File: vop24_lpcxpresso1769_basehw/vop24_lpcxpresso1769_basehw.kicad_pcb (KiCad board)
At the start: 2 copper layers, 105 x 150 mm, 114 parts, among them J1 Micro_SD_Card, J101 Conn_01x03_Male, J201 Screw_Terminal_01x02, J301 USB_B_Micro, J302 Conn_01x06_Male, J303 Conn_01x05_Male, J304 Screw_Terminal_01x02, J401 Conn_01x02, J402 Conn_01x02, J403 Conn_01x02, J404 Conn_01x04, J405 Conn_01x04, J406 Conn_01x04, U1 LPCXpresso1769, U101 MCP1700T-3302E_TT, U102 MCP1700T-3302E_TT, U103 TPS63001, U201 LM358, U301 TPD4S014, U302 LTC4411, U303 LT1512, U401 ADS1292, U402 LM334, U403 LM334, U404 LM334

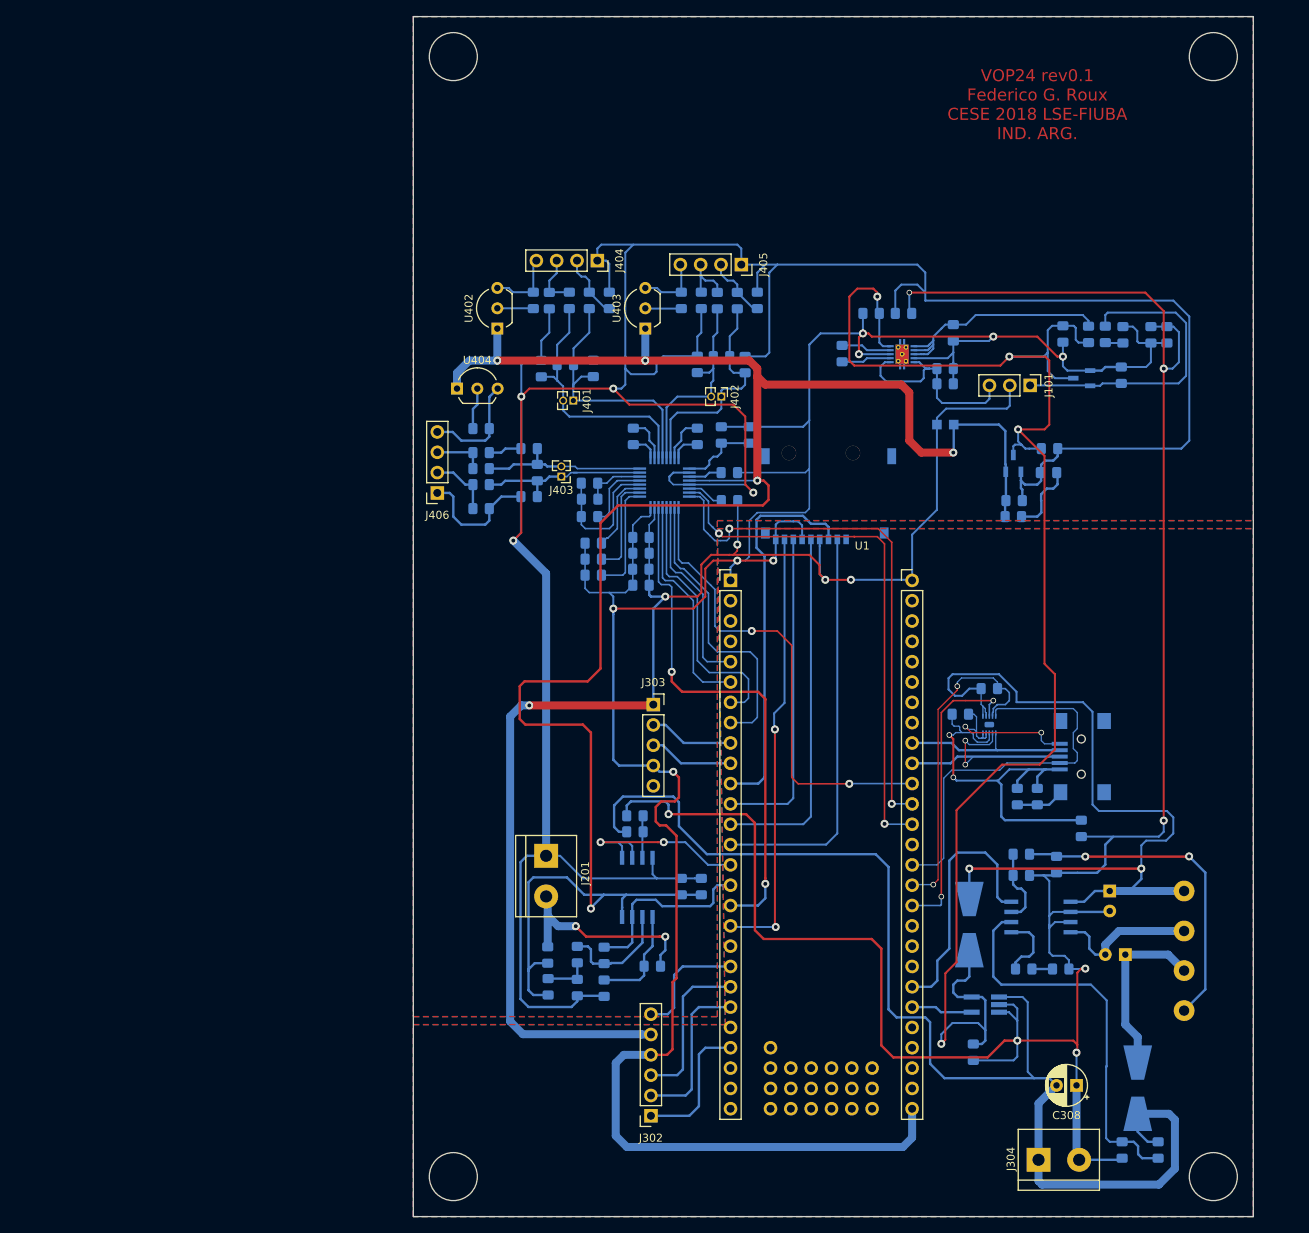
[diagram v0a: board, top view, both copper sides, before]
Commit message: Agregado de leyendas en PCB y ESQ. Agregado de cotas en PCB
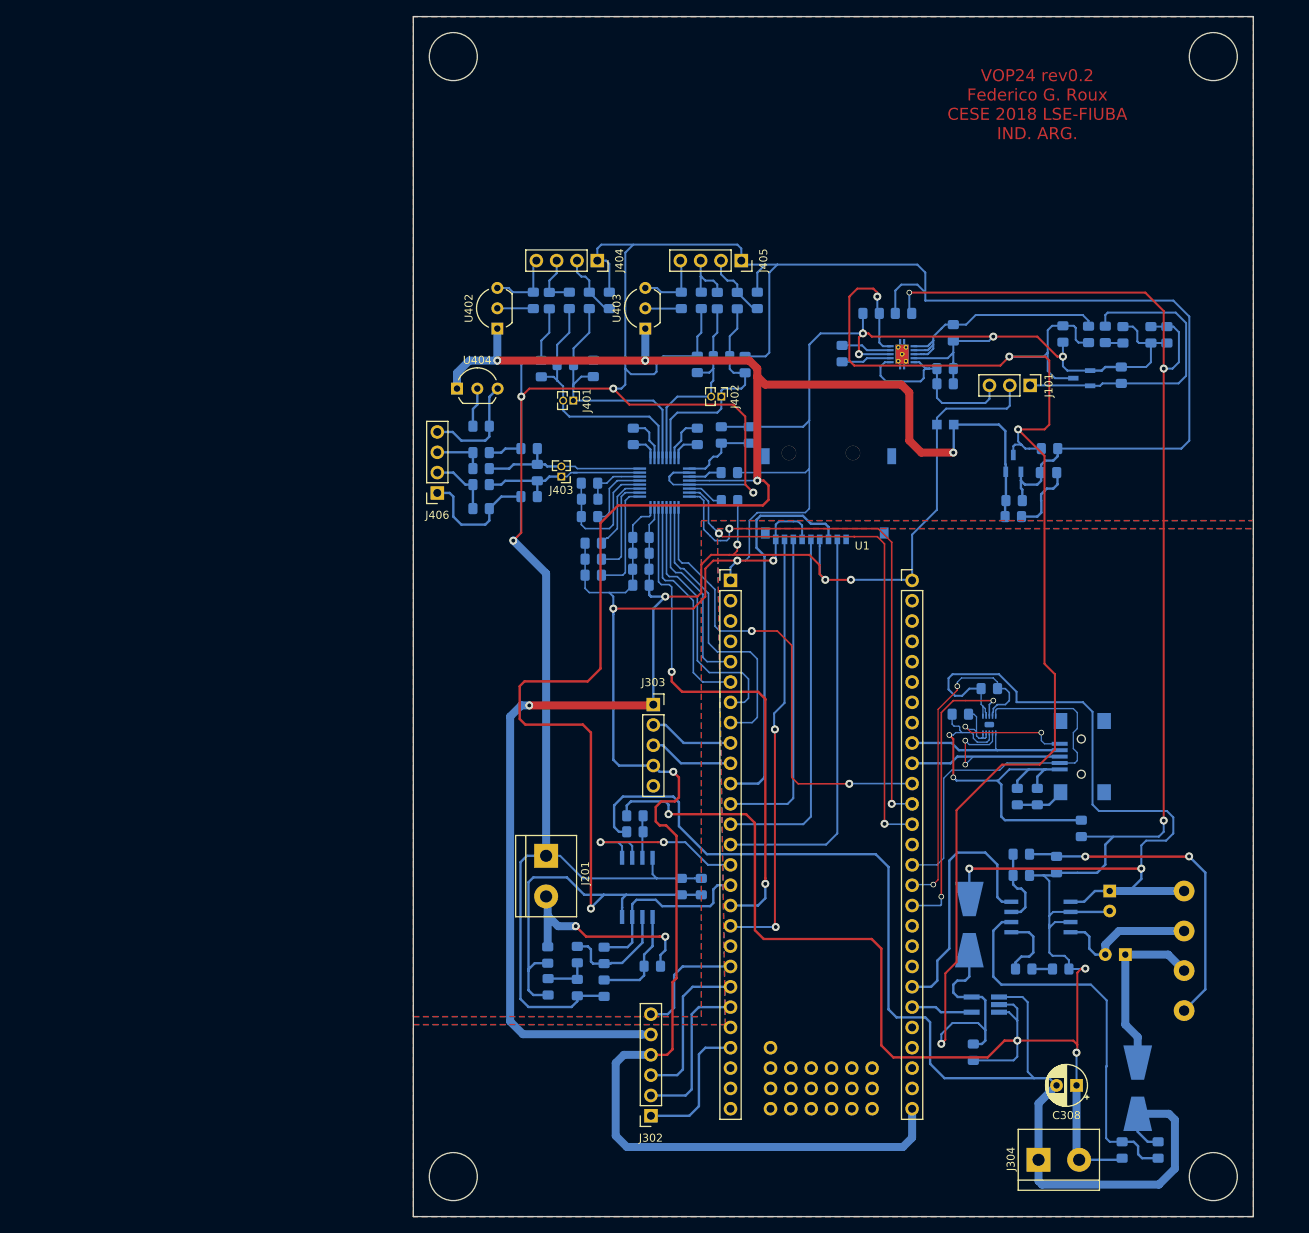
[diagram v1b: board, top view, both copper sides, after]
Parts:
- moved J405 0.50 mm to (81.0, 65.5)
- moved R408 0.30 mm to (48.5, 86.2)
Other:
- board text added: "NOTA SERIGRAFÍA: Como se menciona más arriba, este primer diseño es para realizar en un ROUTER CNC, por lo que no se le dió mucha importancia a la capa de serigrafía porque no se va a realizar. En el diseño final se ubicarán las leyendas de los componentes de una forma más prolija."
- board text added: "NOTA UBICACIÓN COMPONENTES: Los componentes están agrupados por módulo para poder que sea más fácil la inspección a la hora de hacer pruebas, ya que se trata de un prototipo. Además, el hecho de trabajar alrededor de un LPCXpresso hace que el diseño sea más limitado y de mucho mayor tamaño que lo que debería ocupar."
- board text added: "NOTAS CONECTORES: Los conectores J301 y J302 son tiras de pines para conectar directamente los modulos UART-TTL y UART-BLE. No se ubican sobre el borde para que no sobresalgan estas placas hacia afuera, o sobresalgan lo menos posible. El conector miniUSB se ubica lo más cerca del LPCXpresso posible, ya que la conexión no es directa sino a través del STICK, y eso complica la señal de alta velocida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"
- board text added: "NOTAS DE FABRICACION: Este prototipo está diseñado para ser fabricado en un CNC Router para probar las conexiones de cada uno de los módulos. Por ello se usó un solo lado para soldar componentes y minimizar la cantidad de vías. En el siguiente diseño se hará para fabricar en Mayer o Inarci, y se colocará el microcontrolador en lugar del LPCXpresso"
- board text added: "NOTAS DRC: Solamente se marcan los pines no conectados del SHIELD del conector USB, que están cortocircuitados internamente"
- board text added: "TAMAÑO DE PISTAS, VIAS y CLEARANCE: Se crearon las Reglas de Diseño de acuerdo a los estándares de Mayer de 12-10-8-6 mils que se vieron en la cátedra. La mayor parte de la placa está resuelta en el estándar de 8 mils, y en donde se puede, se usaron pistas más grandes."
- board text added: "VOP24 rev0.2 Federico G. Roux CESE 2018 LSE-FIUBA IND. ARG."
- board text removed: "VOP24 rev0.1 Federico G. Roux CESE 2018 LSE-FIUBA IND. ARG."

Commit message: actualizacion de PCB con cambios de ESQ
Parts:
- removed J303: Conn_01x05_Male, Connector_PinSocket_2.54mm:PinSocket_1x05_P2.54mm_Vertical
- removed J304: Screw_Terminal_01x02, TerminalBlock:TerminalBlock_bornier-2_P5.08mm
- removed R101, R102, R103, R303: 0, Resistor_SMD:R_0805_2012Metric_Pad1.15x1.40mm_HandSolder
- added J2: Conn_01x05_Male, Connector_PinSocket_2.54mm:PinSocket_1x05_P2.54mm_Vertical, F.Cu at (-4.67, 125.5)
- added J3: Conn_01x06_Male, Connector_PinSocket_2.54mm:PinSocket_1x06_P2.54mm_Vertical, F.Cu at (-8.27, 125.5)
- added NT101: Net-Tie_2, NetTie:NetTie-2_SMD_Pad0.5mm, F.Cu at (23.8, 126.5)
- added NT102: Net-Tie_2, NetTie:NetTie-2_SMD_Pad0.5mm, F.Cu at (23.8, 124.6)
- added NT103: Net-Tie_2, NetTie:NetTie-2_SMD_Pad0.5mm, F.Cu at (28.2, 124.6)
- added NT301: Net-Tie_2, NetTie:NetTie-2_SMD_Pad0.5mm, F.Cu at (23.8, 133.1)
- added NT302: Net-Tie_2, NetTie:NetTie-2_SMD_Pad0.5mm, F.Cu at (23.8, 135.0)
- added R1: 1k, Resistor_SMD:R_0805_2012Metric_Pad1.15x1.40mm_HandSolder, F.Cu at (3.73, 124.7)
- added S1: B3U-1000P, digikey-footprints:Switch_Tactile_SMD_B3U-1000P, F.Cu at (-0.52, 125.5)
- FB101: value BLM21PG331SN1D -> BLM18PG121SN1D; footprint digikey-footprints:0805 -> digikey-footprints:0603
- J302: value Conn_01x06_Male -> Screw_Terminal_01x02; footprint Connector_PinSocket_2.54mm:PinSocket_1x06_P2.54mm_Vertical -> TerminalBlock:TerminalBlock_bornier-2_P5.08mm
- U301: value TPD4S014 -> LTC4411; footprint meport_kicad_libs:Texas_R-PWSON-N10 -> Package_TO_SOT_SMD:SOT-23-5_HandSoldering
- U302: value LTC4411 -> TPD4S014; footprint Package_TO_SOT_SMD:TSOT-23-5_HandSoldering -> Package_SON:Texas_S-PWSON-N10_ThermalVias
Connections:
- net /ADS1292_esquematico/VCAP1 renamed Net-(C401-Pad1)
- net /ADS1292_esquematico/VCAP2 renamed Net-(C402-Pad1)
- net /ADS1292_esquematico/VREFP renamed Net-(C403-Pad1)
- net /AGND renamed GNDA
- net /CS_ADS renamed /~CS~_ADS
- C101 pad 1: /fuentesLDO/VCC_NREG -> VCOM
- C101 pad 2: /DGND -> GNDD
- C102 pad 1: /fuentesLDO/VCC_NREG -> Net-(C102-Pad1)
- C103 pad 1: /fuentesLDO/VCC_NREG -> VCOM
- C103 pad 2: /DGND -> GNDD
- C104 pad 2: /DGND -> GNDD
- C105 pad 2: /DGND -> GNDD
- C106 pad 1: /AVCC -> VDDA
- C107 pad 2: /DGND -> GNDD
- C108 pad 2: /DGND -> GNDD
- C201 pad 1: /AVCC -> VDDA
- C202 pad 1: /AVCC -> VDDA
- C303 pad 1: /fuentesLDO/VCC_NREG -> VCOM
- C303 pad 2: /analogico/GNDBAT -> GNDREF
- C304 pad 1: /VUSB_OUT -> VBUS
- C304 pad 2: /analogico/GNDBAT -> -BATT
- C306 pad 2: /analogico/GNDBAT -> -BATT
- C308 pad 1: /analogico/GNDBAT -> -BATT
- C308 pad 2: /analogico/VBAT -> +BATT
- C401 pad 2: /DGND -> GNDD
- C402 pad 2: /DGND -> GNDD
- C403 pad 2: /DGND -> GNDD
- C404 pad 2: /DGND -> GNDD
- C405 pad 1: /DVCC -> VDD
- C405 pad 2: /DGND -> GNDD
- C406 pad 1: /DVCC -> VDD
- C406 pad 2: /DGND -> GNDD
- C407 pad 1: /DVCC -> VDD
- C407 pad 2: /DGND -> GNDD
- C408 pad 1: /DVCC -> VDD
- C408 pad 2: /DGND -> GNDD
- D102 pad 2: /AVCC -> VDDA
- D301 pad 1: /fuentesLDO/VCC_NREG -> VCOM
- D301 pad 2: /VUSB_OUT -> VBUS
- D302 pad 1: /analogico/VBAT -> +BATT
- FB101 pad 1: /AVCC -> VCOM
- FB101 pad 2: /DVCC -> Net-(C102-Pad1)
- J1 pad 4: /DVCC -> VDD
- J1 pad 6: /DGND -> GNDD
- J1 pad 9: /DGND -> GNDD
- J101 pad 2: /DVCC -> VDD
- J302 pad 1: /BLE_STATE -> +BATT
- J302 pad 2: /BLE_RXD -> -BATT
- L301 pad 1: /VUSB_OUT -> VBUS
- R104 pad 1: /fuentesLDO/VCC_NREG -> VCOM
- R105 pad 1: /DGND -> GNDD
- R201 pad 1: /AVCC -> VDDA
- R202 pad 2: /analogico/VBAT -> +BATT
- R203 pad 1: /analogico/GNDBAT -> -BATT
- R204 pad 1: /AVCC -> VDDA
- R302 pad 1: /VUSB_OUT -> VBUS
- R304 pad 2: /analogico/GNDBAT -> -BATT
- R306 pad 1: /analogico/GNDBAT -> -BATT
- R307 pad 2: /analogico/VBAT -> +BATT
- R308 pad 1: /analogico/GNDBAT -> -BATT
- R401 pad 1: /ADS1292_esquematico/RLDINV -> /ADS1292_esquematico/RLDIN
- R401 pad 2: /ADS1292_esquematico/RLDIN -> /ADS1292_esquematico/RLDINV
- R403 pad 1: /DGND -> GNDD
- R404 pad 1: /DVCC -> VDD
- R405 pad 1: /DGND -> GNDD
- U1 pad 1: /DGND -> GNDD
- U1 pad 23: Net-(U1-Pad23) -> /BLE_STATE
- U1 pad 24: /BLE_STATE -> Net-(U1-Pad24)
- U1 pad 28: /DVCC -> VDD
- U1 pad 54: /DGND -> GNDD
- U101 pad 2: /AVCC -> VDDA
- U101 pad 3: /fuentesLDO/VCC_NREG -> Net-(C102-Pad1)
- U102 pad 1: /DGND -> GNDD
- U102 pad 3: /fuentesLDO/VCC_NREG -> VCOM
- U103 pad 3: /DGND -> GNDD
- U103 pad 5: /fuentesLDO/VCC_NREG -> VCOM
- U103 pad 9: /DGND -> GNDD
- U201 pad 8: /AVCC -> VDDA
- U301 pad 1: /VUSB_OUT -> +BATT
- U301 pad 2: /VUSB_OUT -> -BATT
- U301 pad 3: /TPD_~EN -> -BATT
- U301 pad 4: /TPD_~ACK -> /LTC4411_STAT
- U301 pad 5: /USB_ID -> VCOM
- U302 pad 1: /analogico/VBAT -> VBUS
- U302 pad 2: /analogico/GNDBAT -> Net-(U302-Pad2)
- U302 pad 3: /analogico/GNDBAT -> /TPD_~EN
- U302 pad 4: /LTC4411_STAT -> /TPD_~ACK
- U302 pad 5: /fuentesLDO/VCC_NREG -> /USB_ID
- U303 pad 5: /VUSB_OUT -> VBUS
- U303 pad 6: /analogico/GNDBAT -> -BATT
- U303 pad 7: /analogico/GNDBAT -> -BATT
- U401 pad 12: /AVCC -> VDDA
- U401 pad 23: /DVCC -> VDD
- U401 pad 24: /DGND -> GNDD
- U402 pad 1: /AVCC -> VDDA
- U403 pad 1: /AVCC -> VDDA
- U404 pad 1: /AVCC -> VDDA
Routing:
- net GNDD: track 0.00 -> 326.4 mm, vias 0 -> 8
- net /DGND: track 326.4 -> 0.00 mm, vias 8 -> 0
- net VDDA: track 0.00 -> 261.9 mm, vias 0 -> 5
- net /AVCC: track 261.9 -> 0.00 mm, vias 5 -> 0
- net VDD: track 0.00 -> 110.8 mm, vias 0 -> 4
- net /DVCC: track 185.7 -> 74.9 mm, vias 5 -> 1
- net /fuentesLDO/VCC_NREG: track 198.9 -> 191.4 mm
- net VCOM: track 0.00 -> 7.49 mm
- removed copper zone on B.Cu, net /DGND
- removed copper zone on F.Cu, net /DGND
- removed copper zone on B.Cu, net GNDA
- removed copper zone on F.Cu, net GNDA
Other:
- board text added: "Notas de Grilla: Grid: 0,1mm"
